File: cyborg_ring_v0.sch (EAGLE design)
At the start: 44 parts, among them U1 ATTINYX5V-LEFT, U2 ATTINYX5V-RIGHT

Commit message: Board
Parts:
- removed RCON10, RCON3, RCON4, RCON9: R0805-1/2, cyborg_ring:R0805-1/2
- added PAD: TPTP06R, testpad:TPTP06R
- added RCON15, RCON16: R0805-1/2TEST2, cyborg_ring:R0805-1/2TEST2
- C1: device rcl:C-EUC0402K -> rcl:C-EUC0201
- GND, MISO, MOSI, RST, SCK, VCC: value TPTP20R -> TPTP15R; device testpad:TPTP20R -> testpad:TPTP15R
- RCON1, RCON11, RCON12, RCON13, RCON14, RCON2, RCON7, RCON8: value R0805-1/2 -> R0805-1/2TEST; device cyborg_ring:R0805-1/2 -> cyborg_ring:R0805-1/2TEST
- RCON5, RCON6: value R0805-1/2 -> R0805-1/2TEST2; device cyborg_ring:R0805-1/2 -> cyborg_ring:R0805-1/2TEST2
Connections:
- net LED_R0 renamed R0
- net LED_R1 renamed R1
- removed net LEDL_L1: MOSI.TP
- removed net LED_L0: LED_CON1.P$1, LED_CON3.P$1, LED_CON5.P$1, LED_CON7.P$1, SCK.TP, U1.PB2
- removed net LED_L1: LED_CON11.P$1, LED_CON13.P$1, LED_CON15.P$1, LED_CON9.P$1, U1.PB0
- removed net N$11: U$2.+, U$3.-
- removed net SWITCH: MISO.TP, SW1.P$1, U1.PB1
- new net MISO/SW: MISO.TP, RCON13.P$1, U1.PB1
- new net MOSI/L1: LED_CON1.P$1, LED_CON3.P$1, LED_CON5.P$1, LED_CON7.P$1, MOSI.TP, U1.PB0
- new net SCK/L0: LED_CON11.P$1, LED_CON13.P$1, LED_CON15.P$1, LED_CON9.P$1, SCK.TP, U1.PB2
- new net SWITCH1: RCON14.P$1, SW1.P$2
- new net VCC": RCON16.P$1, RCON8.P$1
- new net VCC/2: RCON6.P$1, U$2.+, U$3.-
- new net VCC/2": RCON5.P$1
- net GND: now also PAD.TP; no longer RCON13.P$1, RCON3.P$1, RCON5.P$1, RCON7.P$1, RCON9.P$1, SW1.P$2
- net GND1: now also SW1.P$1; no longer RCON10.P$1, RCON14.P$1, RCON4.P$1, RCON6.P$1, RCON8.P$1
- net VCC: now also RCON15.P$1, RCON7.P$1
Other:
- moved on the sheet: RCON11, RCON12, RCON13, RCON14, SW1

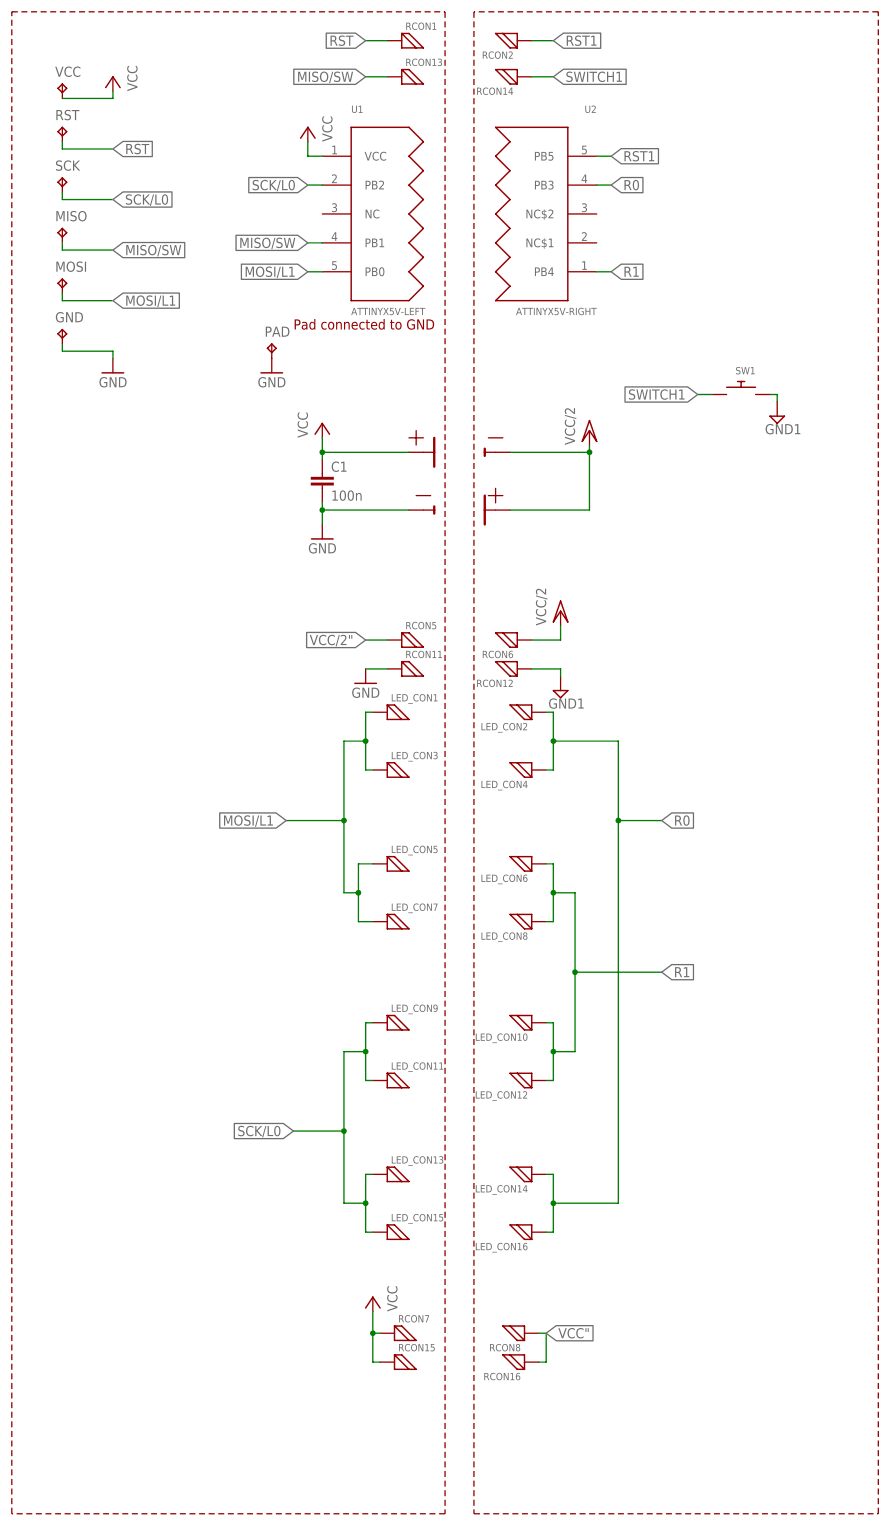
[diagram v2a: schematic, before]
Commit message: Clearer schematic
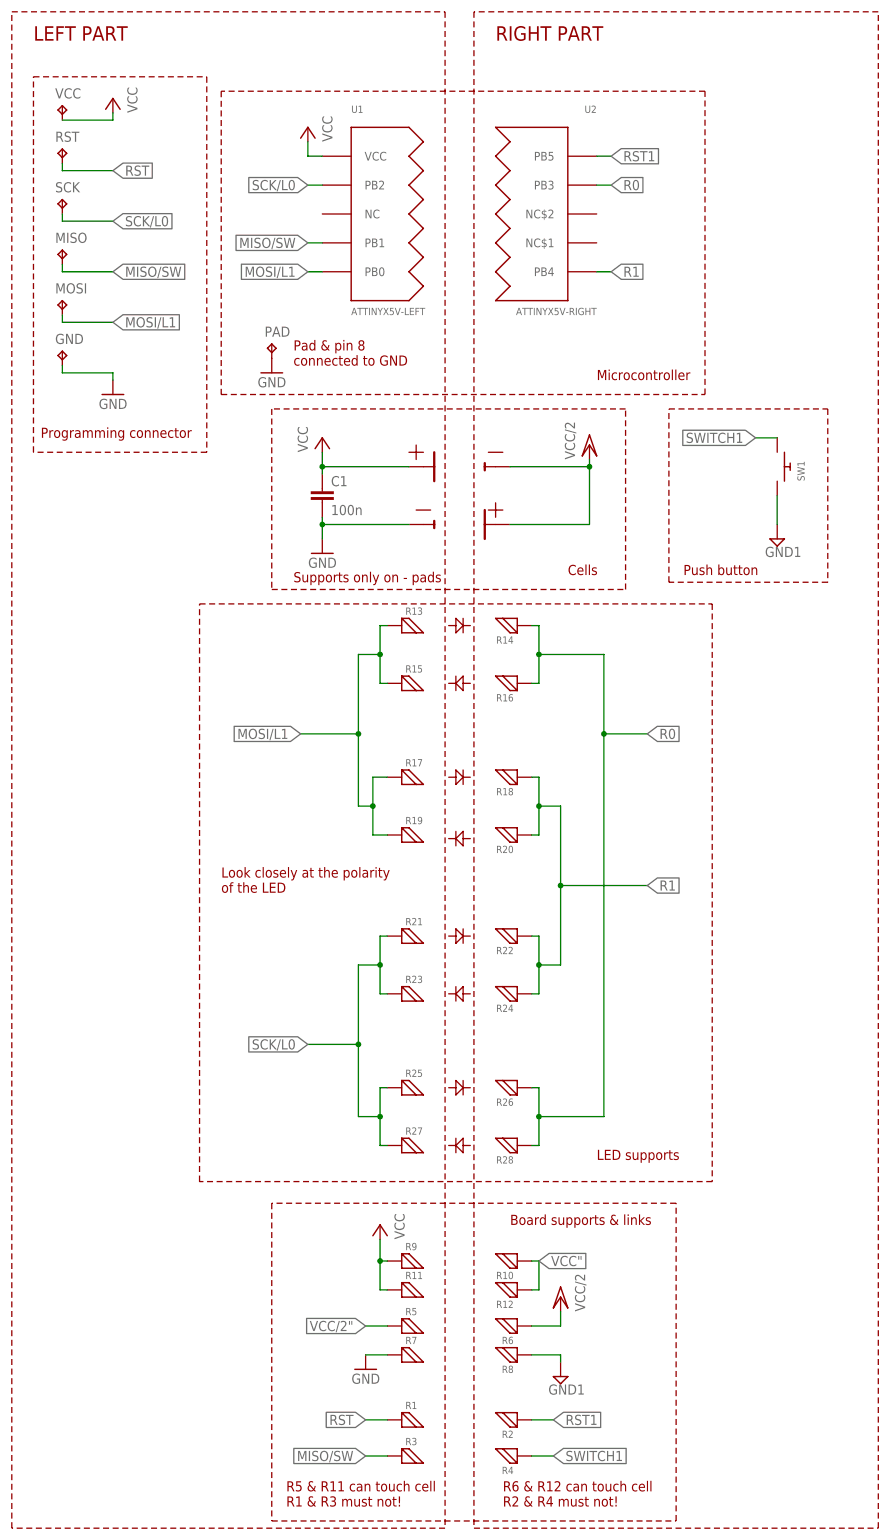
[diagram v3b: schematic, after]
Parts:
- removed LED_CON1, LED_CON10, LED_CON11, LED_CON12, LED_CON13, LED_CON14, LED_CON15, LED_CON16, LED_CON2, LED_CON3, LED_CON4, LED_CON5, LED_CON6, LED_CON7, LED_CON8, LED_CON9: R0508-1/2, cyborg_ring:R0508-1/2
- removed RCON1, RCON11, RCON12, RCON13, RCON14, RCON2, RCON7, RCON8: R0805-1/2TEST, cyborg_ring:R0805-1/2TEST
- removed RCON15, RCON16, RCON5, RCON6: R0805-1/2TEST2, cyborg_ring:R0805-1/2TEST2
- added R1, R10, R2, R3, R4, R7, R8, R9: R0805-1/2TEST, cyborg_ring:R0805-1/2TEST
- added R11, R12, R5, R6: R0805-1/2TEST2, cyborg_ring:R0805-1/2TEST2
- added R13, R14, R15, R16, R17, R18, R19, R20, R21, R22, R23, R24, R25, R26, R27, R28: R0508-1/2, cyborg_ring:R0508-1/2
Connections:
- net GND: now also R7.P$1; no longer RCON11.P$1
- net GND1: now also R8.P$1; no longer RCON12.P$1
- net MISO/SW: now also R3.P$1; no longer RCON13.P$1
- net MOSI/L1: now also R13.P$1, R15.P$1, R17.P$1, R19.P$1; no longer LED_CON1.P$1, LED_CON3.P$1, LED_CON5.P$1, LED_CON7.P$1
- net R0: now also R14.P$1, R16.P$1, R26.P$1, R28.P$1; no longer LED_CON14.P$1, LED_CON16.P$1, LED_CON2.P$1, LED_CON4.P$1
- net R1: now also R18.P$1, R20.P$1, R22.P$1, R24.P$1; no longer LED_CON10.P$1, LED_CON12.P$1, LED_CON6.P$1, LED_CON8.P$1
- net RST: now also R1.P$1; no longer RCON1.P$1
- net RST1: now also R2.P$1; no longer RCON2.P$1
- net SCK/L0: now also R21.P$1, R23.P$1, R25.P$1, R27.P$1; no longer LED_CON11.P$1, LED_CON13.P$1, LED_CON15.P$1, LED_CON9.P$1
- net SWITCH1: now also R4.P$1; no longer RCON14.P$1
- net VCC: now also R11.P$1, R9.P$1; no longer RCON15.P$1, RCON7.P$1
- net VCC": now also R10.P$1, R12.P$1; no longer RCON16.P$1, RCON8.P$1
- net VCC/2: now also R6.P$1; no longer RCON6.P$1
- net VCC/2": now also R5.P$1; no longer RCON5.P$1
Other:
- note added: "Board supports & links"
- note added: "Cells"
- note added: "LED supports"
- note added: "LEFT PART"
- note added: "Look closely at the polarity of the LED"
- note added: "Microcontroller"
- note added: "Pad & pin 8 connected to GND"
- note added: "Programming connector"
- note added: "Push button"
- note added: "R5 & R11 can touch cell R1 & R3 must not!"
- note added: "R6 & R12 can touch cell R2 & R4 must not!"
- note added: "RIGHT PART"
- note added: "Supports only on - pads"
- note removed: "Pad connected to GND"
- moved on the sheet: C1, GND, MISO, MOSI, RST, SCK, SW1, VCC
